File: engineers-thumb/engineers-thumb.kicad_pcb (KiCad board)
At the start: 2 copper layers, 55.1 x 56.8 mm, 46 parts, among them J1 power, J2 Conn_01x06_Female, Q1 BC556, U1 LM13700, U2 TL074

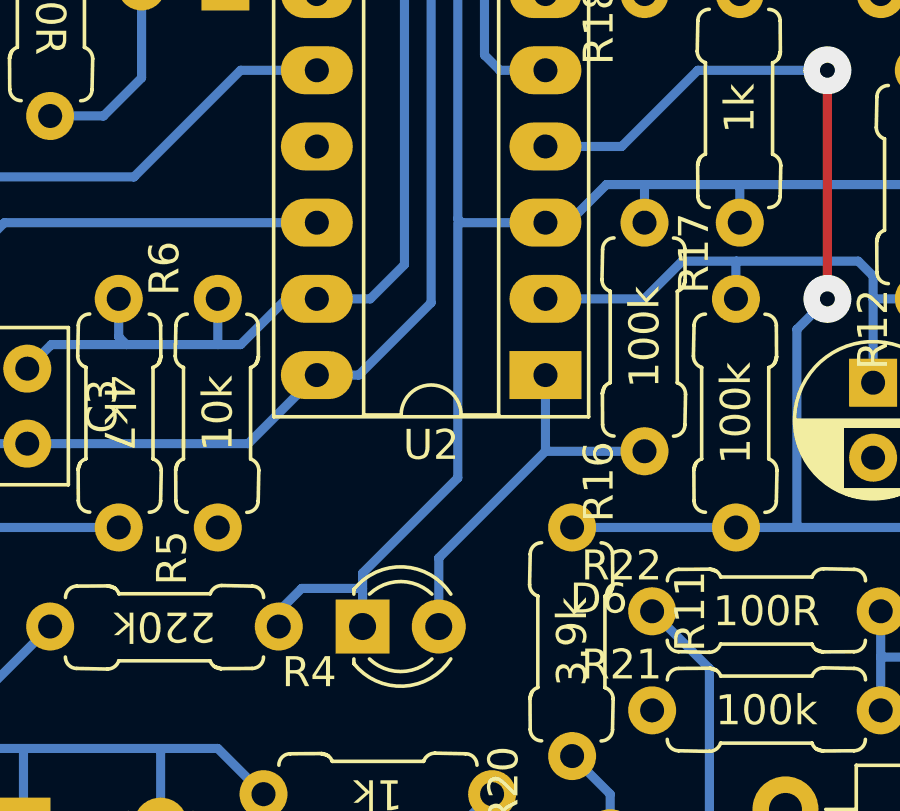
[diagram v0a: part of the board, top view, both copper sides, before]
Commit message: Added compressor and psu schematics.
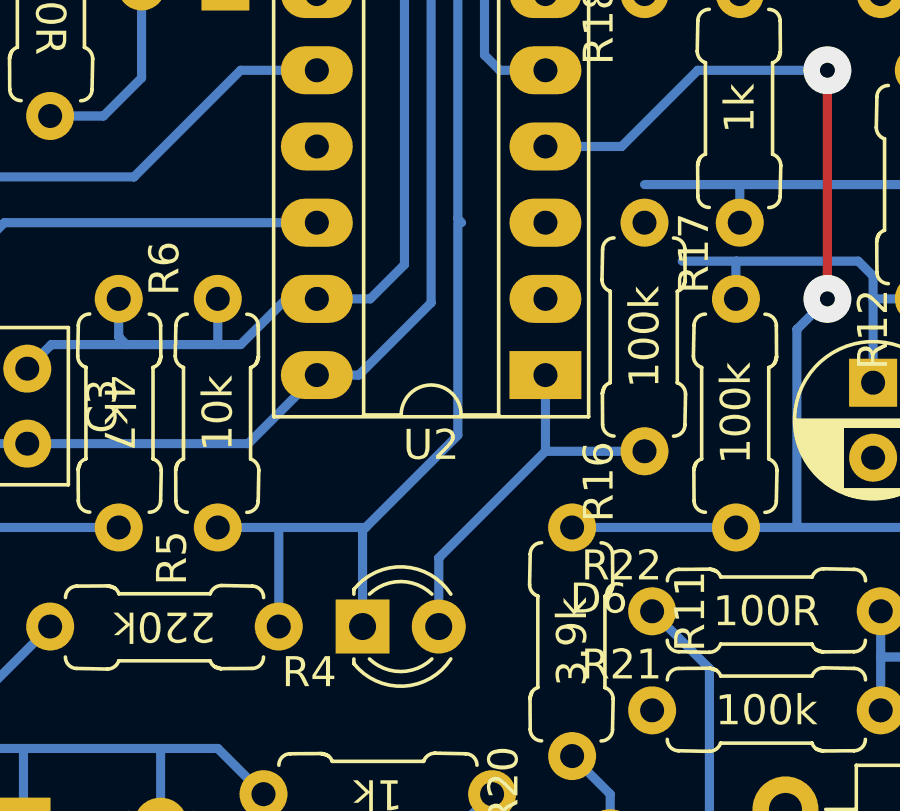
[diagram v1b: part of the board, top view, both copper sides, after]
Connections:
- R5 pad 1: GND -> +4.5V
- U2 pad 2: Net-(C4-Pad1) -> +4.5V
- U2 pad 3: +4.5V -> Net-(C4-Pad1)
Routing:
- net Net-(C4-Pad1): track 18.0 -> 13.7 mm
- net +4.5V: track 87.9 -> 84.6 mm
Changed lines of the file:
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@@
     (fp_line (start 0.66 -1.25) (end 0.66 1.25) (layer "F.Fab") (width 0.1))
     (pad "1" thru_hole circle (at 0 0 90) (size 1.6 1.6) (drill 0.8) (layers *.Cu *.Mask)
-      (net 2 "GND") (pintype "passive"))
+      (net 7 "+4.5V") (pintype "passive"))
     (pad "2" thru_hole oval (at 7.62 0 90) (size 1.6 1.6) (drill 0.8) (layers *.Cu *.Mask)
       (net 24 "/fb_return") (pintype "passive"))
@@
       (net 12 "Net-(D6-Pad2)") (pintype "output"))
     (pad "2" thru_hole oval locked (at 0 2.54 180) (size 2.4 1.6) (drill 0.8) (layers *.Cu *.Mask)
-      (net 25 "Net-(C4-Pad1)") (pinfunction "-") (pintype "input"))
+      (net 7 "+4.5V") (pinfunction "-") (pintype "input"))
     (pad "3" thru_hole oval locked (at 0 5.08 180) (size 2.4 1.6) (drill 0.8) (layers *.Cu *.Mask)
-      (net 7 "+4.5V") (pinfunction "+") (pintype "input"))
+      (net 25 "Net-(C4-Pad1)") (pinfunction "+") (pintype "input"))
     (pad "4" thru_hole oval locked (at 0 7.62 180) (size 2.4 1.6) (drill 0.8) (layers *.Cu *.Mask)
       (net 1 "+9V") (pinfunction "V+") (pintype "power_in"))
@@
   (segment (start 239.141 83.693) (end 241.554 86.106) (width 0.3048) (layer "B.Cu") (net 6))
   (segment (start 241.554 86.106) (end 241.554 88.138) (width 0.3048) (layer "B.Cu") (net 6))
-  (segment (start 208.28 88.392) (end 206.248 88.392) (width 0.3048) (layer "B.Cu") (net 7))
   (segment (start 237.49 71.882) (end 229.87 71.882) (width 0.3048) (layer "B.Cu") (net 7))
-  (segment (start 214.376 76.2) (end 211.582 76.2) (width 0.3048) (layer "B.Cu") (net 7))
+  (segment (start 205.486 86.36) (end 203.454 86.36) (width 0.3048) (layer "B.Cu") (net 7))
   (segment (start 240.494 72.644) (end 240.538 72.6) (width 0.3048) (layer "B.Cu") (net 7))
-  (segment (start 208.28 88.392) (end 208.28 87.884) (width 0.3048) (layer "B.Cu") (net 7))
   (segment (start 229.362 71.882) (end 226.314 74.93) (width 0.3048) (layer "B.Cu") (net 7))
   (segment (start 213.36 57.658) (end 229.87 57.658) (width 0.3048) (layer "B.Cu") (net 7))
-  (segment (start 205.486 89.154) (end 205.486 89.662) (width 0.3048) (layer "B.Cu") (net 7))
+  (segment (start 208.28 86.4616) (end 208.3816 86.36) (width 0.3048) (layer "B.Cu") (net 7))
   (segment (start 220.726 74.93) (end 217.678 74.93) (width 0.3048) (layer "B.Cu") (net 7))
+  (segment (start 208.28 89.662) (end 208.28 86.4616) (width 0.3048) (layer "B.Cu") (net 7))
   (segment (start 229.87 71.882) (end 229.362 71.882) (width 0.3048) (layer "B.Cu") (net 7))
+  (segment (start 211.455 76.2) (end 211.455 83.2866) (width 0.3048) (layer "B.Cu") (net 7))
   (segment (start 220.853 76.2) (end 220.853 74.93) (width 0.3048) (layer "B.Cu") (net 7))
-  (segment (start 215.138 76.2) (end 214.376 76.2) (width 0.3048) (layer "B.Cu") (net 7))
-  (segment (start 208.28 89.662) (end 208.28 88.392) (width 0.3048) (layer "B.Cu") (net 7))
+  (segment (start 211.455 83.2866) (end 208.3816 86.36) (width 0.3048) (layer "B.Cu") (net 7))
   (segment (start 237.49 71.882) (end 238.76 71.882) (width 0.3048) (layer "B.Cu") (net 7))
-  (segment (start 217.678 76.2) (end 217.678 74.93) (width 0.3048) (layer "B.Cu") (net 7))
   (segment (start 211.455 76.073) (end 211.455 59.563) (width 0.3048) (layer "B.Cu") (net 7))
   (segment (start 238.76 71.882) (end 239.522 72.644) (width 0.3048) (layer "B.Cu") (net 7))
-  (segment (start 208.28 87.884) (end 211.455 84.709) (width 0.3048) (layer "B.Cu") (net 7))
-  (segment (start 217.678 74.93) (end 216.408 74.93) (width 0.3048) (layer "B.Cu") (net 7))
-  (segment (start 211.455 84.709) (end 211.455 76.2) (width 0.3048) (layer "B.Cu") (net 7))
-  (segment (start 216.408 74.93) (end 215.138 76.2) (width 0.3048) (layer "B.Cu") (net 7))
+  (segment (start 205.486 89.662) (end 205.486 86.36) (width 0.3048) (layer "B.Cu") (net 7))
   (segment (start 211.455 59.563) (end 213.36 57.658) (width 0.3048) (layer "B.Cu") (net 7))
-  (segment (start 206.248 88.392) (end 205.486 89.154) (width 0.3048) (layer "B.Cu") (net 7))
   (segment (start 211.582 76.2) (end 211.455 76.073) (width 0.3048) (layer "B.Cu") (net 7))
   (segment (start 226.314 74.93) (end 220.726 74.93) (width 0.3048) (layer "B.Cu") (net 7))
+  (segment (start 208.3816 86.36) (end 205.486 86.36) (width 0.3048) (layer "B.Cu") (net 7))
   (segment (start 239.522 72.644) (end 240.494 72.644) (width 0.3048) (layer "B.Cu") (net 7))
   (segment (start 202.438 61.722) (end 206.756 66.04) (width 0.3048) (layer "B.Cu") (net 8))
@@
   (segment (start 220.726 77.496578) (end 220.739289 77.483289) (width 0.3048) (layer "B.Cu") (net 25))
   (segment (start 224.803289 77.483289) (end 225.298 77.978) (width 0.3048) (layer "B.Cu") (net 25))
-  (segment (start 217.678 78.74) (end 218.934711 77.483289) (width 0.3048) (layer "B.Cu") (net 25))
+  (segment (start 215.138 76.2) (end 214.376 76.2) (width 0.3048) (layer "B.Cu") (net 25))
   (segment (start 226.822 78.74) (end 225.298 78.74) (width 0.3048) (layer "B.Cu") (net 25))
   (segment (start 218.934711 77.483289) (end 220.739289 77.483289) (width 0.3048) (layer "B.Cu") (net 25))
   (segment (start 220.726 78.74) (end 220.726 77.496578) (width 0.3048) (layer "B.Cu") (net 25))
-  (segment (start 214.376 78.74) (end 217.678 78.74) (width 0.3048) (layer "B.Cu") (net 25))
   (segment (start 225.298 77.978) (end 225.298 78.74) (width 0.3048) (layer "B.Cu") (net 25))
   (segment (start 204.898 58.848) (end 200.994 58.848) (width 0.3048) (layer "B.Cu") (net 26))
